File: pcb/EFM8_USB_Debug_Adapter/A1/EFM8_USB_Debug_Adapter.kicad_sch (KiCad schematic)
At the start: 36 parts, among them J100 EFM8_IDC_Debug_Header_Horizon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, J110 2137160001, J111 TTL-232R_Header_Horizontal, J120 31230102, J130 EFM8_USB_8-Bit_Debug_Header_H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, J131 Header_01x02_Wurth_61300211121, M110 USB_Light_Pipe, M120 PSU_Light_Pipe, M130 DBG8_Light_Pipe, Q110 SI3443CDV-T1-GE3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

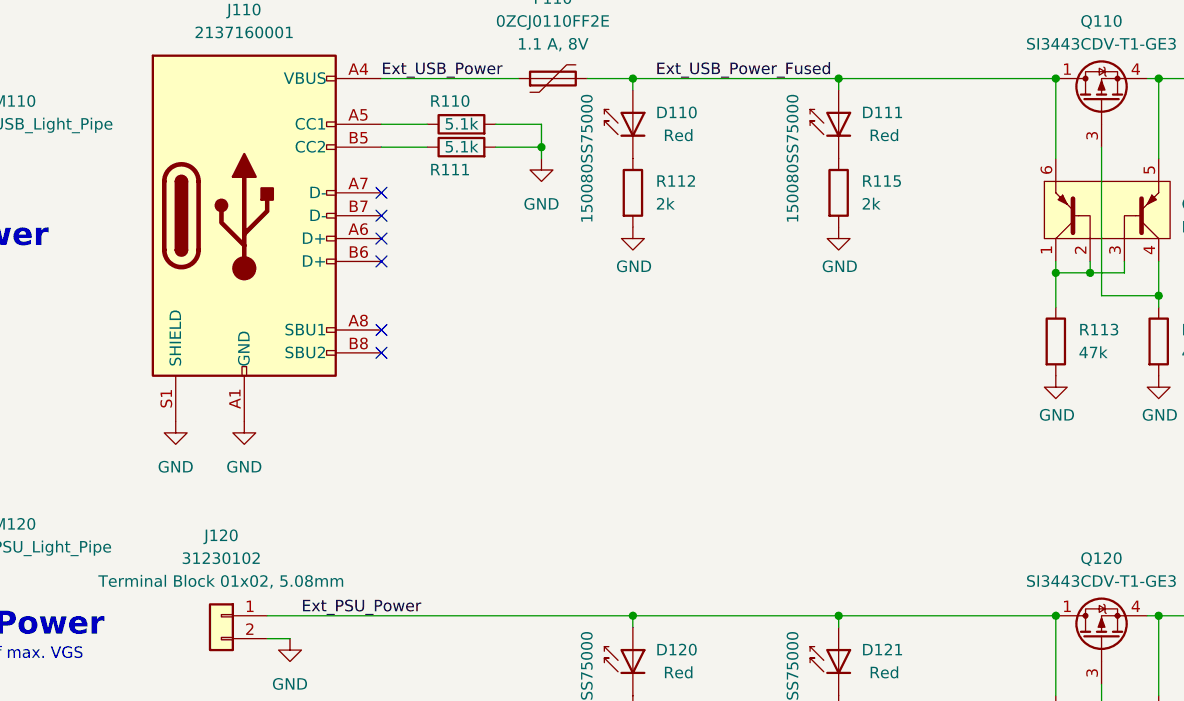
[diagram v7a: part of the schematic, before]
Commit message: Update to KiCad 7, add Cura projects
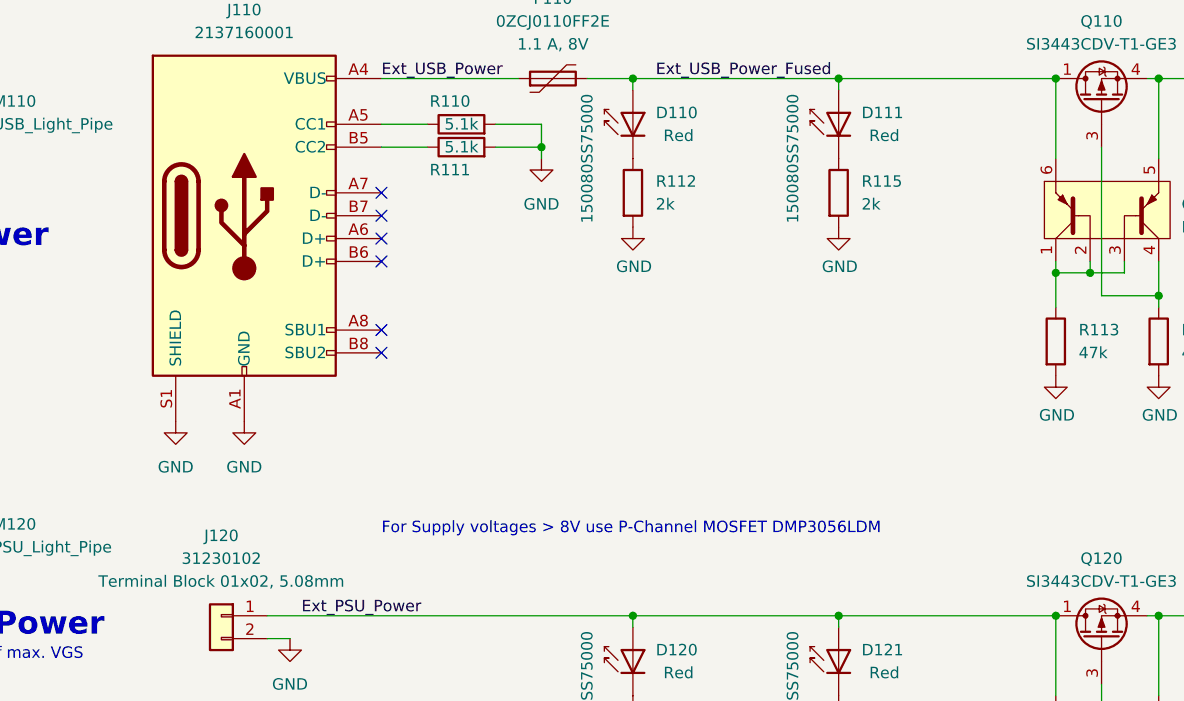
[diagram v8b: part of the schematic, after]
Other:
- note added: "For Supply voltages > 8V use P-Channel MOSFET DMP3056LDM"
